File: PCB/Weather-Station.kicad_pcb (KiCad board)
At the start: 2 copper layers, 10 parts, among them J1 Biruta, J2 Power, J3 BH1750-FVI, J4 BME280, J5 Pluviometro, J6 Anamometro, U1 NodeMCU1.0(ESP-12E)

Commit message: Adicionando Gerber
Signed-off-by: Gustavo Costa <gustavocosta@ic.ufal.br>
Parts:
- J6: value Anamometro -> Anemometro
- moved J3 10.9 mm to (179.2, 34.4)
- moved J6 10.8 mm to (179.2, 80.0)
- moved J4 10.8 mm to (179.2, 51.4)
- moved J5 10.8 mm to (179.2, 70.5)
- moved J2 8.72 mm to (130.0, 77.0)
- moved J1 8.64 mm to (130.0, 44.0)
- moved R1 7.61 mm to (136.5, 42.5), turned to 270 degrees
- moved R2 2.57 mm to (172.5, 58.0), turned to 90 degrees
- moved R3 2.03 mm to (172.5, 63.5), turned to 90 degrees
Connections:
- net Net-(J2-Pad1) renamed +5V
- J1 pad 1: Net-(J1-Pad1) -> +3V3
- J2 pad 2: Net-(J2-Pad2) -> GND
- J3 pad 1: Net-(J3-Pad1) -> +3V3
- J3 pad 5: Net-(J3-Pad5) -> GND
- J4 pad 1: Net-(J3-Pad1) -> +3V3
- J4 pad 2: Net-(J3-Pad5) -> GND
- J4 pad 5: Net-(J3-Pad1) -> +3V3
- J4 pad 6: Net-(J3-Pad1) -> +3V3
- J5 pad 1: Net-(J3-Pad1) -> +3V3
- J6 pad 1: Net-(J3-Pad1) -> +3V3
- R1 pad 2: Net-(R1-Pad2) -> GND
- R2 pad 2: Net-(J3-Pad5) -> GND
- R3 pad 2: Net-(J3-Pad5) -> GND
- U1 pad 10: Net-(R1-Pad2) -> GND
- U1 pad 11: Net-(J1-Pad1) -> +3V3
- U1 pad 14: Net-(J2-Pad2) -> GND
- U1 pad 16: Net-(J3-Pad1) -> +3V3
- U1 pad 17: Net-(J3-Pad5) -> GND
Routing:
- net +3V3: track 0.00 -> 114.2 mm
- net Net-(J3-Pad2): track 0.00 -> 33.9 mm, vias 0 -> 1
- net Net-(J3-Pad3): track 0.00 -> 33.5 mm
- net Net-(J6-Pad2): track 0.00 -> 28.5 mm
- net Net-(J5-Pad2): track 0.00 -> 23.1 mm
- net +5V: track 0.00 -> 10.7 mm
- net Net-(J1-Pad2): track 0.00 -> 10.6 mm
- net GND: track 0.00 -> 3.90 mm, vias 0 -> 3
- added copper zone on B.Cu, net GND
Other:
- board outline added: 56 x 59 mm
- net class Default: clearance 0.2 -> 0.1524; trace_width 0.25 -> 0.1524; via_dia 0.6 -> 0.508; via_drill 0.4 -> 0.3302
- net class PWR added: clearance 0.1524, trace_width 0.3, via_dia 0.508, via_drill 0.3302
- rule trace_clearance: 0.2 -> 0.1524
- rule trace_min: 0.2 -> 0.14
- board text added: "Anemometro"
- board text added: "BH1750-FVI"
- board text added: "BME280"
- board text added: "Biruta"
- board text added: "Pluviometro"
- board text added: "Power"

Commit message: Refazendo PCB
Signed-off-by: Gustavo Costa <gustavocosta@ic.ufal.br>
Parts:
- added C1: 100nF, Capacitors_SMD:C_0805, F.Cu at (150.5, 97.5)
- added J7: FTDI, Pin_Headers:Pin_Header_Straight_1x04_Pitch2.54mm, F.Cu at (230.5, 83.1)
- added R4: 10K, Resistors_SMD:R_0805, F.Cu at (158.3, 107.8)
- added R5: 10K, Resistors_SMD:R_0805, F.Cu at (152.6, 107.2)
- added R6: 10K, Resistors_SMD:R_0805, F.Cu at (152.4, 111.2)
- added R7: 10K, Resistors_SMD:R_0805, F.Cu at (158.3, 112.0)
- added R8: 10K, Resistors_SMD:R_0805, F.Cu at (156.8, 117.8)
- added SW1: SW_Push_SPDT, Buttons_Switches_ThroughHole:SW_Micro_SPST, F.Cu at (203.0, 111.5)
- added SW2: SW_Push, Buttons_Switches_THT:SW_PUSH_6mm, F.Cu at (195.0, 82.8)
- added SW3: SW_DIP_x01, Buttons_Switches_ThroughHole:SW_Micro_SPST, F.Cu at (213.0, 111.2)
- added U2: ESP-12E, ESP8266:ESP-12E, F.Cu at (200.2, 90.0)
- U1: value NodeMCU1.0(ESP-12E) -> AP1117-33; footprint ESP8266_l2:NodeMCU1.0(12-E) -> TO_SOT_Packages_SMD:SOT-223-3_TabPin2
- moved J3 88.9 mm to (230.2, 107.2)
- moved J1 67.8 mm to (181.0, 88.8)
- moved J4 64.6 mm to (230.2, 91.1)
- moved U1 60.2 mm to (192.5, 108.5), turned to 270 degrees
- moved J2 59.1 mm to (181.0, 106.8)
- moved R1 59.0 mm to (157.3, 97.8), turned to 0 degrees
- moved R2 46.7 mm to (158.6, 102.5), turned to 0 degrees
- moved R3 43.2 mm to (151.8, 101.5), turned to 0 degrees
- moved J5 24.3 mm to (181.0, 94.8), turned to 90 degrees
- moved J6 20.6 mm to (181.0, 100.5), turned to 90 degrees
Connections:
- J2 pad 1: +5V -> GND
- J2 pad 2: GND -> Net-(J2-Pad2)
- J5 pad 1: +3V3 -> Net-(J5-Pad1)
- J5 pad 2: Net-(J5-Pad2) -> +3V3
- J6 pad 1: +3V3 -> Net-(J6-Pad1)
- J6 pad 2: Net-(J6-Pad2) -> +3V3
- R2 pad 1: Net-(J5-Pad2) -> GND
- R2 pad 2: GND -> Net-(J5-Pad1)
- R3 pad 1: Net-(J6-Pad2) -> Net-(J6-Pad1)
- U1 pad 1: Net-(J1-Pad2) -> GND
- U1 pad 2: (no net) -> Net-(SW1-Pad1)
- U1 pad 3: (no net) -> Net-(J2-Pad2)
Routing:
- net +3V3: track 114.2 -> 0.00 mm
- net Net-(J3-Pad2): track 33.9 -> 0.00 mm, vias 1 -> 0
- net Net-(J3-Pad3): track 33.5 -> 0.00 mm
- net Net-(J6-Pad2): track 28.5 -> 0.00 mm
- net Net-(J5-Pad2): track 23.1 -> 0.00 mm
- net +5V: track 10.7 -> 0.00 mm
- net Net-(J1-Pad2): track 10.6 -> 0.00 mm
- net GND: track 3.90 -> 0.00 mm, vias 3 -> 0
- removed copper zone on B.Cu, net GND
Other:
- board outline removed
- board text removed: "Anemometro"
- board text removed: "BH1750-FVI"
- board text removed: "BME280"
- board text removed: "Biruta"
- board text removed: "Pluviometro"
- board text removed: "Power"

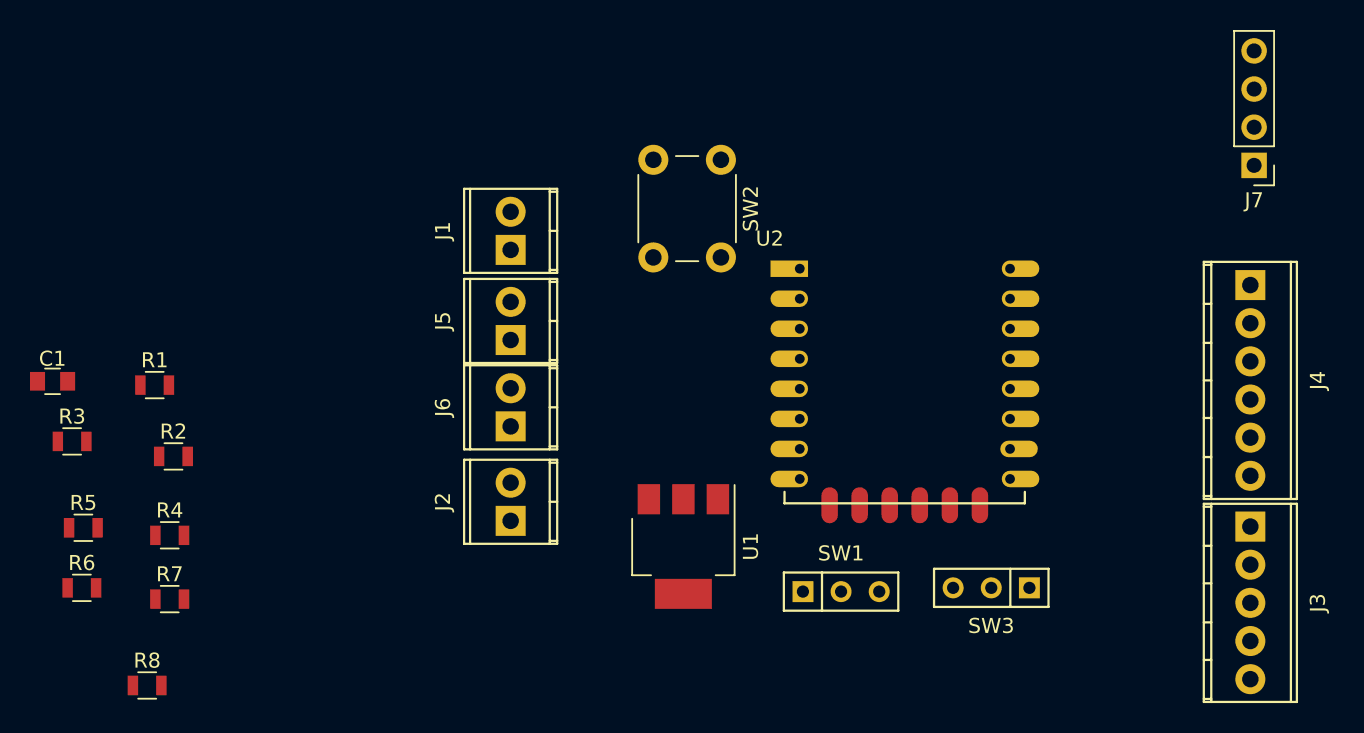
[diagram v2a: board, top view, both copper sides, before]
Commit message: Ajustando os valores da biruta
Signed-off-by: Gustavo Costa <gustavocosta@ic.ufal.br>
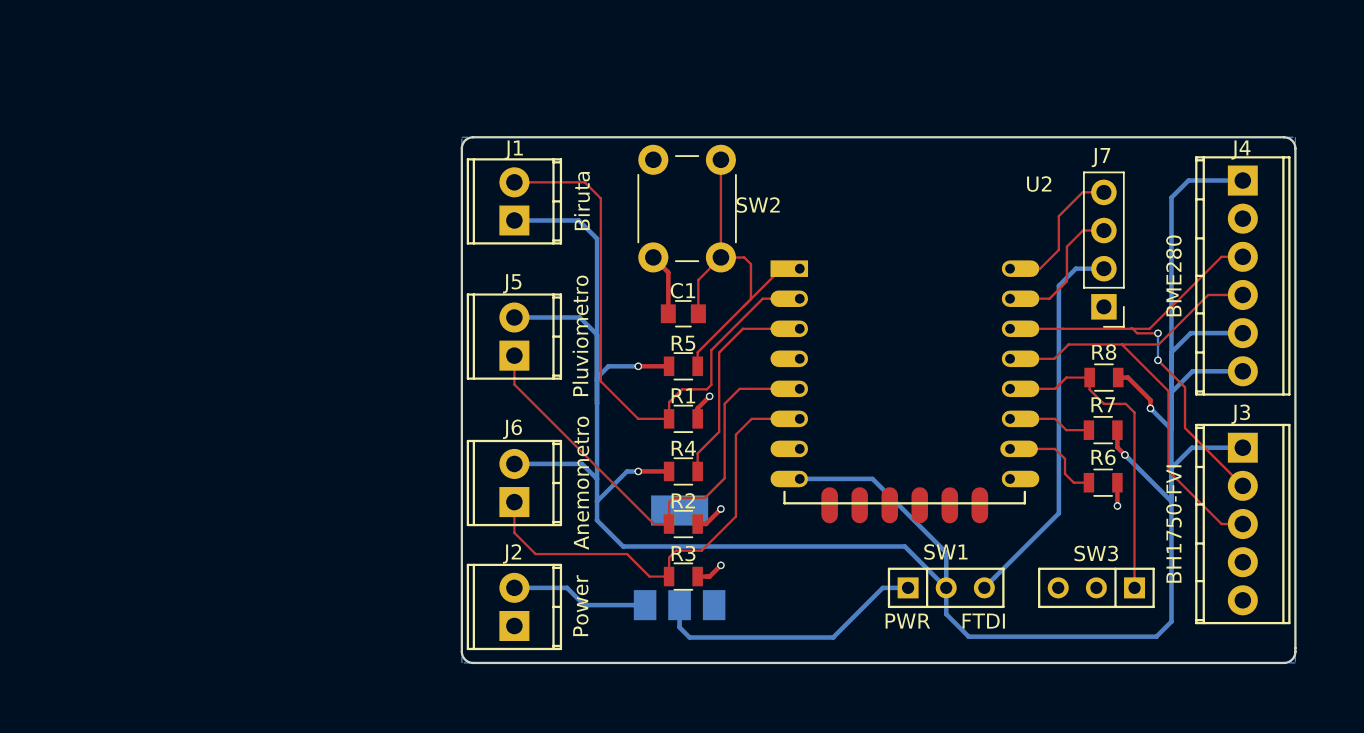
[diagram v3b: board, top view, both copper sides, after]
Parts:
- U1: footprint TO_SOT_Packages_SMD:SOT-223-3_TabPin2 -> TO_SOT_Packages_SMD:SOT-223; moved to B.Cu
- moved R6 68.4 mm to (220.4, 104.2)
- moved R8 66.9 mm to (220.5, 97.2)
- moved R7 63.2 mm to (220.4, 100.8)
- moved C1 42.2 mm to (192.5, 93.0)
- moved R3 41.7 mm to (192.5, 110.5)
- moved R5 41.4 mm to (192.5, 96.5), turned to 180 degrees
- moved R1 35.3 mm to (192.5, 100.0)
- moved R4 34.5 mm to (192.5, 103.5), turned to 180 degrees
- moved R2 34.2 mm to (192.5, 107.0), turned to 180 degrees
- moved J7 13.7 mm to (220.5, 92.5)
- moved J2 7.00 mm to (181.2, 113.8)
- moved SW1 7.00 mm to (210.0, 111.2)
- moved SW3 7.00 mm to (220.0, 111.2)
- moved J4 6.98 mm to (229.8, 84.1)
- moved J3 5.27 mm to (229.8, 101.9)
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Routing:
- net +3V3: track 0.00 -> 177.1 mm, vias 0 -> 4
- net Net-(J1-Pad2): track 0.00 -> 38.0 mm
- net Net-(J3-Pad3): track 0.00 -> 33.4 mm
- net Net-(J5-Pad1): track 0.00 -> 32.2 mm
- net Net-(J3-Pad2): track 0.00 -> 31.9 mm, vias 0 -> 2
- net Net-(J6-Pad1): track 0.00 -> 30.5 mm
- net Net-(C1-Pad2): track 0.00 -> 26.1 mm
- net Net-(J7-Pad2): track 0.00 -> 25.6 mm
- net Net-(R8-Pad1): track 0.00 -> 21.7 mm
- net Net-(SW1-Pad1): track 0.00 -> 18.3 mm
- net Net-(R4-Pad1): track 0.00 -> 14.5 mm
- net GND: track 0.00 -> 11.4 mm, vias 0 -> 4
- net TXD: track 0.00 -> 9.67 mm
- net RXD: track 0.00 -> 9.49 mm
- net Net-(J2-Pad2): track 0.00 -> 9.18 mm
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- added copper zone on B.Cu, net GND
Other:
- board outline added: 55.5 x 35 mm
- board text added: "Anemometro"
- board text added: "BH1750-FVI"
- board text added: "BME280"
- board text added: "Biruta"
- board text added: "FTDI"
- board text added: "PWR"
- board text added: "Pluviometro"
- board text added: "Power"

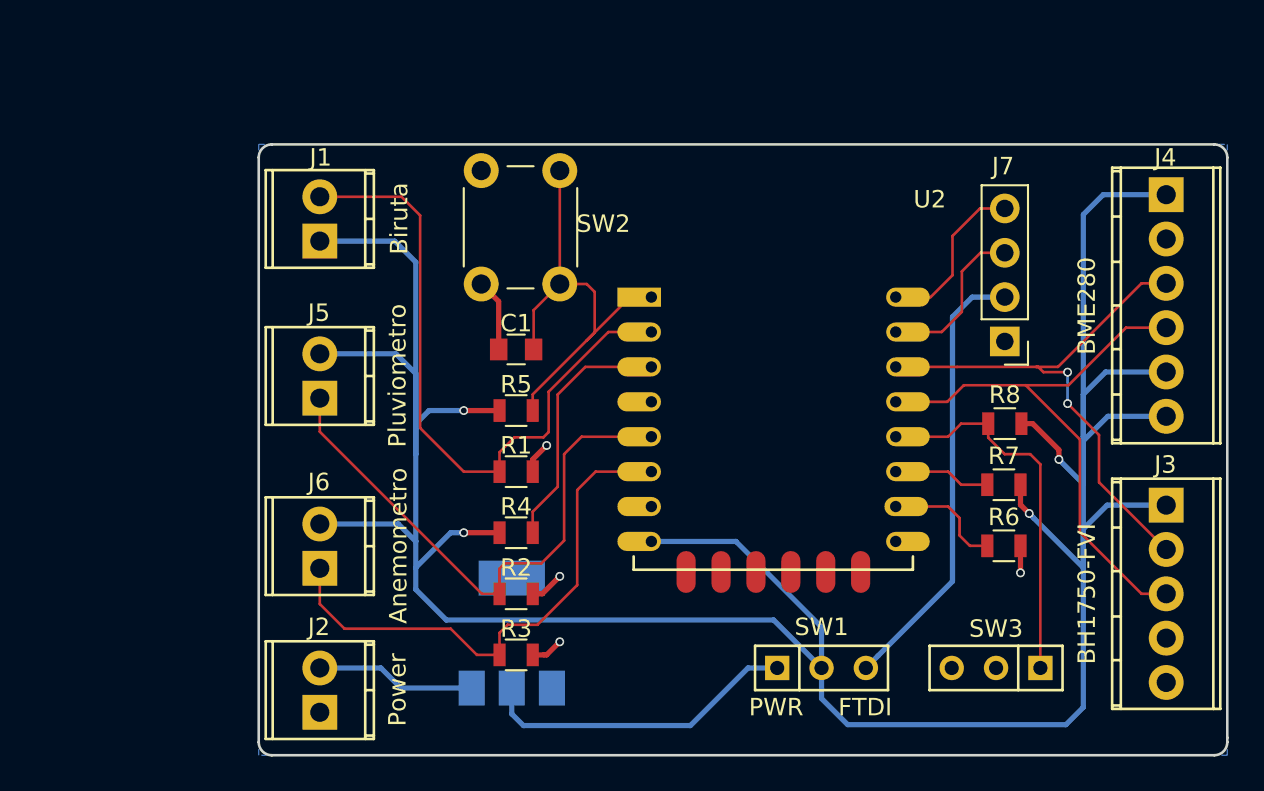
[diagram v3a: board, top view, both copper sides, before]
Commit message: Iniciada a PCB com ESP32 devkit
Signed-off-by: Gustavo Costa <gustavocosta@ic.ufal.br>
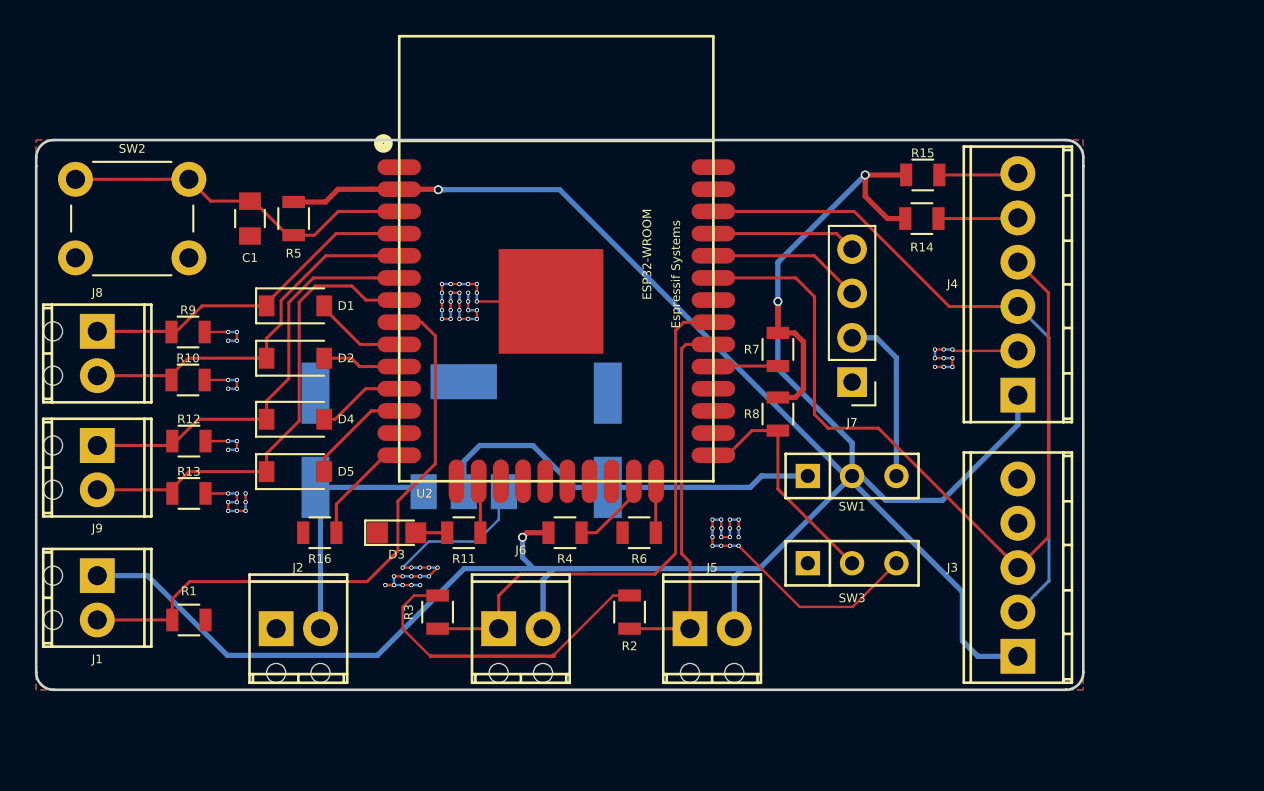
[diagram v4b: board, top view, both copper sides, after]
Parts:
- added C2: 22μF, Capacitors_SMD:CP_Elec_6.3x7.7, B.Cu at (181.0, 98.2)
- added C3: 22μF, Capacitors_SMD:CP_Elec_6.3x7.7, B.Cu at (197.8, 98.2)
- added D1: D, Diodes_SMD:D_SOD-123, F.Cu at (179.8, 90.5)
- added D2: D, Diodes_SMD:D_SOD-123, F.Cu at (179.8, 93.5)
- added D3: LED, LEDs:LED_0805, F.Cu at (185.7, 103.5)
- added D4: D, Diodes_SMD:D_SOD-123, F.Cu at (179.8, 97.0)
- added D5: D, Diodes_SMD:D_SOD-123, F.Cu at (179.8, 100.0)
- added J8: Conn_01x02, TerminalBlock_Phoenix:TerminalBlock_Phoenix_MPT-2.54mm_2pol, F.Cu at (168.5, 92.0)
- added J9: Conn_01x02, TerminalBlock_Phoenix:TerminalBlock_Phoenix_MPT-2.54mm_2pol, F.Cu at (168.5, 98.5)
- added R10: 1.5K, Resistors_SMD:R_0805, F.Cu at (173.7, 94.8)
- added R11: 330, Resistors_SMD:R_0805, F.Cu at (189.5, 103.5)
- added R12: 1.5K, Resistors_SMD:R_0805, F.Cu at (173.8, 98.2)
- added R13: 1.5K, Resistors_SMD:R_0805, F.Cu at (173.8, 101.2)
- added R14: 10K, Resistors_SMD:R_0805, F.Cu at (215.8, 85.5)
- added R15: 10K, Resistors_SMD:R_0805, F.Cu at (215.8, 83.0)
- added R16: 10K, Resistors_SMD:R_0805, F.Cu at (181.2, 103.5)
- added R9: 1.5K, Resistors_SMD:R_0805, F.Cu at (173.7, 92.0)
- J1, J2, J5, J6: footprint Terminal_Blocks:TerminalBlock_Pheonix_MPT-2.54mm_2pol -> TerminalBlock_Phoenix:TerminalBlock_Phoenix_MPT-2.54mm_2pol
- J3: footprint Terminal_Blocks:TerminalBlock_Pheonix_MPT-2.54mm_5pol -> TerminalBlock_Phoenix:TerminalBlock_Phoenix_MPT-2.54mm_5pol
- J4: footprint Terminal_Blocks:TerminalBlock_Pheonix_MPT-2.54mm_6pol -> TerminalBlock_Phoenix:TerminalBlock_Phoenix_MPT-2.54mm_6pol
- SW3: value SW_DIP_x01 -> SW_SPDT
- U2: value ESP-12E -> ESP-32S; footprint ESP8266:ESP-12E -> MPPT_Library:ESP32-WROOM
- moved SW2 27.8 mm to (167.2, 83.2), turned to 0 degrees
- moved J5 25.0 mm to (202.5, 109.0), turned to 0 degrees
- moved J1 23.0 mm to (168.5, 106.0), turned to 270 degrees
- moved R6 20.9 mm to (199.6, 103.5), turned to 180 degrees
- moved R1 20.6 mm to (173.8, 108.5)
- moved C1 17.0 mm to (177.2, 85.5), turned to 90 degrees
- moved R5 16.8 mm to (179.8, 85.5), turned to 90 degrees
- moved R7 15.1 mm to (207.5, 93.0), turned to 270 degrees
- moved J4 14.3 mm to (221.2, 95.6), turned to 90 degrees
- moved R8 13.0 mm to (207.5, 96.7), turned to 90 degrees
- moved J3 12.1 mm to (221.2, 110.6), turned to 90 degrees
- moved U1 11.6 mm to (189.5, 98.0)
- moved SW1 11.1 mm to (211.8, 100.2)
- moved J6 10.8 mm to (191.5, 109.0), turned to 0 degrees
- moved SW3 10.2 mm to (211.8, 105.2), turned to 0 degrees
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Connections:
- J1 pad 2: Net-(J1-Pad2) -> ADC1_CH4
- J4 pad 5: +3V3 -> Net-(J4-Pad5)
- J4 pad 6: +3V3 -> Net-(J4-Pad6)
- R1 pad 1: Net-(J1-Pad2) -> ADC1_CH4
- R7 pad 1: Net-(R7-Pad1) -> +3V3
- R7 pad 2: +3V3 -> Net-(R7-Pad2)
- SW3 pad 1: Net-(R8-Pad1) -> (no net)
- SW3 pad 2: GND -> Net-(R8-Pad1)
- SW3 pad 3: (no net) -> GND
- U2 pad 1: Net-(C1-Pad2) -> GND
- U2 pad 10: Net-(R6-Pad1) -> GPIO25
- U2 pad 11: Net-(R7-Pad1) -> GPIO26
- U2 pad 12: Net-(R8-Pad1) -> GPIO27
- U2 pad 13: Net-(J3-Pad3) -> (no net)
- U2 pad 14: Net-(J3-Pad2) -> Net-(R16-Pad1)
- U2 pad 15: RXD -> GND
- U2 pad 16: TXD -> Net-(R11-Pad1)
- U2 pad 2: Net-(J1-Pad2) -> +3V3
- U2 pad 3: Net-(R4-Pad1) -> Net-(C1-Pad2)
- U2 pad 4: (no net) -> ADC1_CH0
- U2 pad 5: Net-(J5-Pad1) -> ADC1_CH3
- U2 pad 6: Net-(J6-Pad1) -> ADC1_CH6
- U2 pad 7: (no net) -> ADC1_CH7
- U2 pad 8: +3V3 -> ADC1_CH4
- U2 pad 9: GND -> GPIO33
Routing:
- net GND: track 11.4 -> 91.7 mm, vias 4 -> 86
- net Net-(J1-Pad2): track 38.0 -> 0.00 mm
- net ADC1_CH4: track 0.00 -> 35.2 mm
- net ADC1_CH7: track 0.00 -> 27.4 mm
- net ADC1_CH6: track 0.00 -> 24.5 mm
- net ADC1_CH3: track 0.00 -> 22.0 mm
- net ADC1_CH0: track 0.00 -> 19.7 mm
- net Net-(J7-Pad2): track 25.6 -> 9.79 mm
- net Net-(J3-Pad3): track 33.4 -> 47.2 mm
- net +3V3: track 177.1 -> 165.8 mm
- net Net-(J5-Pad1): track 32.2 -> 21.6 mm
- net Net-(R4-Pad1): track 14.5 -> 4.69 mm
- net Net-(R8-Pad1): track 21.7 -> 13.6 mm
- net Net-(J3-Pad2): track 31.9 -> 38.7 mm, vias 2 -> 0
- net Net-(R16-Pad1): track 0.00 -> 6.47 mm
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- added copper zone on F.Cu, net GND
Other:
- board size 55.5 x 35 mm -> 60 x 31.5 mm
- net class Default: trace_width 0.1524 -> 0.175
- net class GND added: clearance 0.1524, trace_width 0.14, via_dia 0.25, via_drill 0.15
- net class PWR: via_dia 0.508 -> 0.52; via_drill 0.3302 -> 0.335
- rule via_min_drill: 0.3 -> 0.15
- rule via_min_size: 0.4 -> 0.25
- board text removed: "Anemometro"
- board text removed: "BH1750-FVI"
- board text removed: "BME280"
- board text removed: "Biruta"
- board text removed: "FTDI"
- board text removed: "PWR"
- board text removed: "Pluviometro"
- board text removed: "Power"
